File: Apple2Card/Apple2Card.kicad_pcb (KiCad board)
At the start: 2 copper layers, 160 x 78.2 mm, 60 parts, among them J1 ICSP, J2 Conn_01x25, J3 Conn_01x25, J4 Conn_01x16, J5 Conn_01x08, J6 WIZNET 5500, SW1 SW_Push, U1 ATmega328P-P, U3 74HCT00, U4 82C55A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

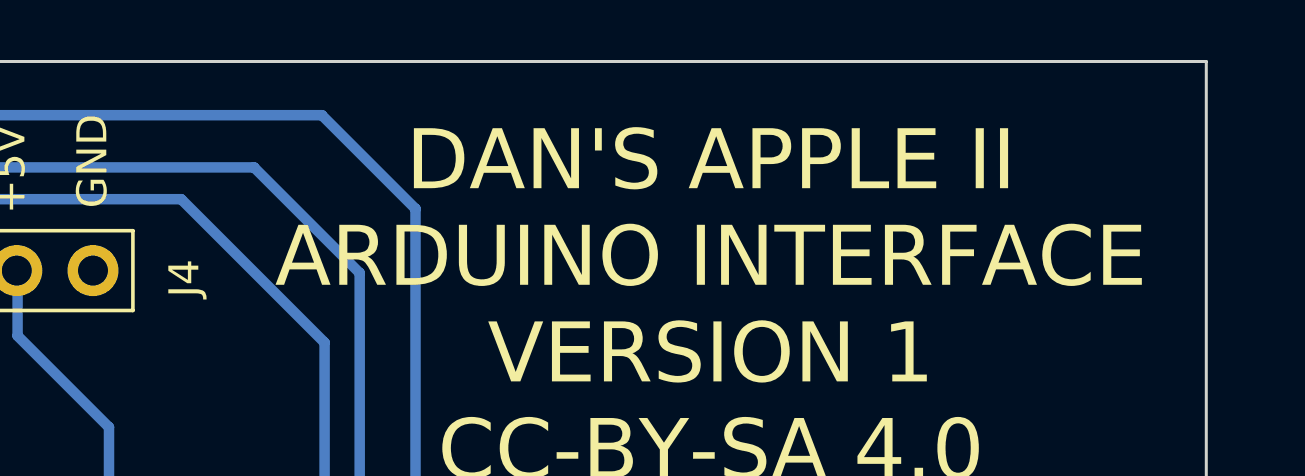
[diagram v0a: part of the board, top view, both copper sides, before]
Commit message: Fixed memory overallocation problem in Arduinosketch
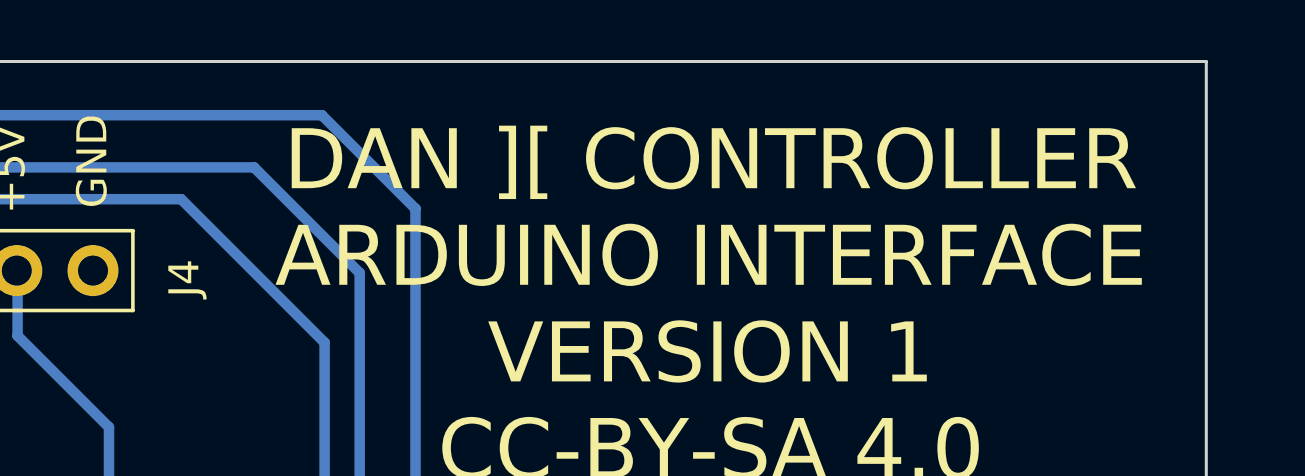
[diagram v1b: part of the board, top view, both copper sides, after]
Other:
- board text added: "DAN ][ CONTROLLER ARDUINO INTERFACE VERSION 1 CC-BY-SA 4.0"
- board text removed: "DAN'S APPLE II ARDUINO INTERFACE VERSION 1 CC-BY-SA 4.0"
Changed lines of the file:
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@@
     (effects (font (size 1 1) (thickness 0.15)))
   )
-  (gr_text "DAN'S APPLE II\nARDUINO INTERFACE\nVERSION 1\nCC-BY-SA 4.0" (at 176.53 33.528) (layer "F.SilkS")
+  (gr_text "DAN ][ CONTROLLER\nARDUINO INTERFACE\nVERSION 1\nCC-BY-SA 4.0" (at 176.53 33.528) (layer "F.SilkS")
     (effects (font (size 2 2) (thickness 0.25)))
   )

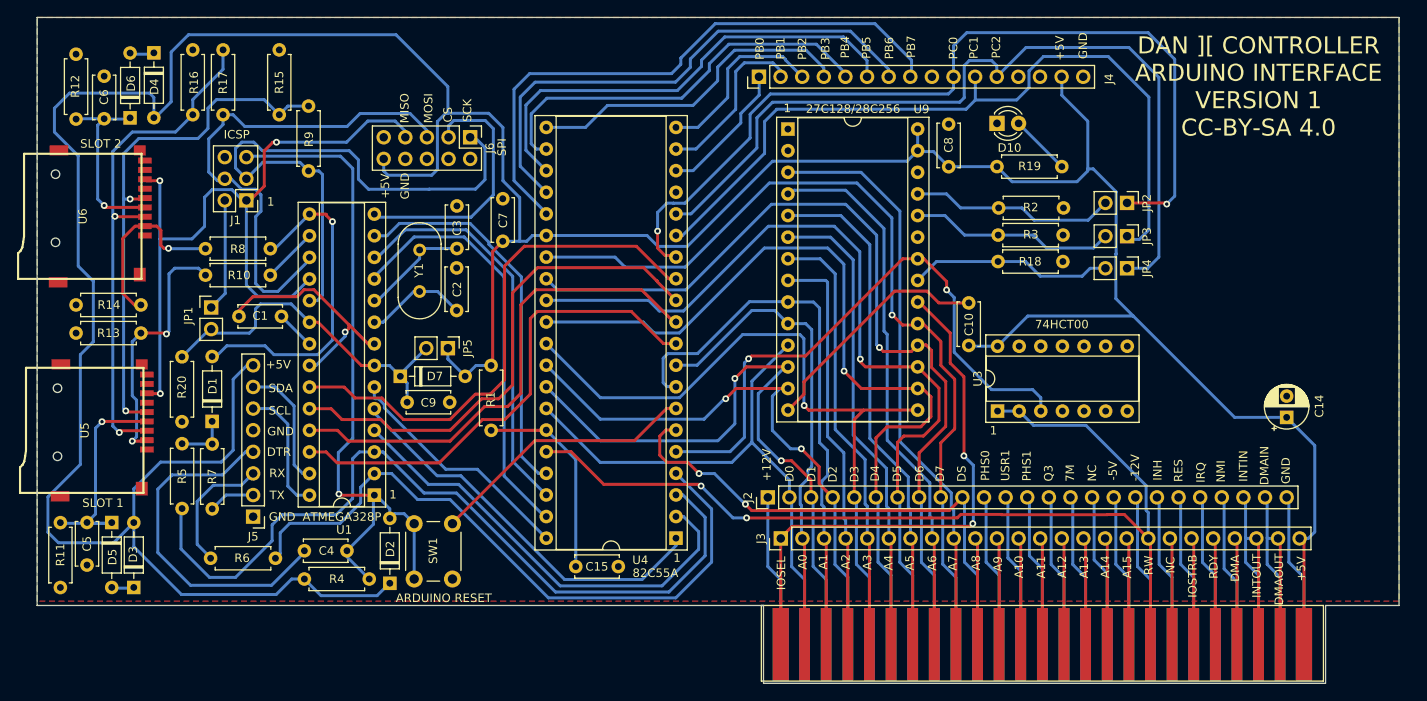
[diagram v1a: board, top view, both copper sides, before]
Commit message: Fixed reset circuitry
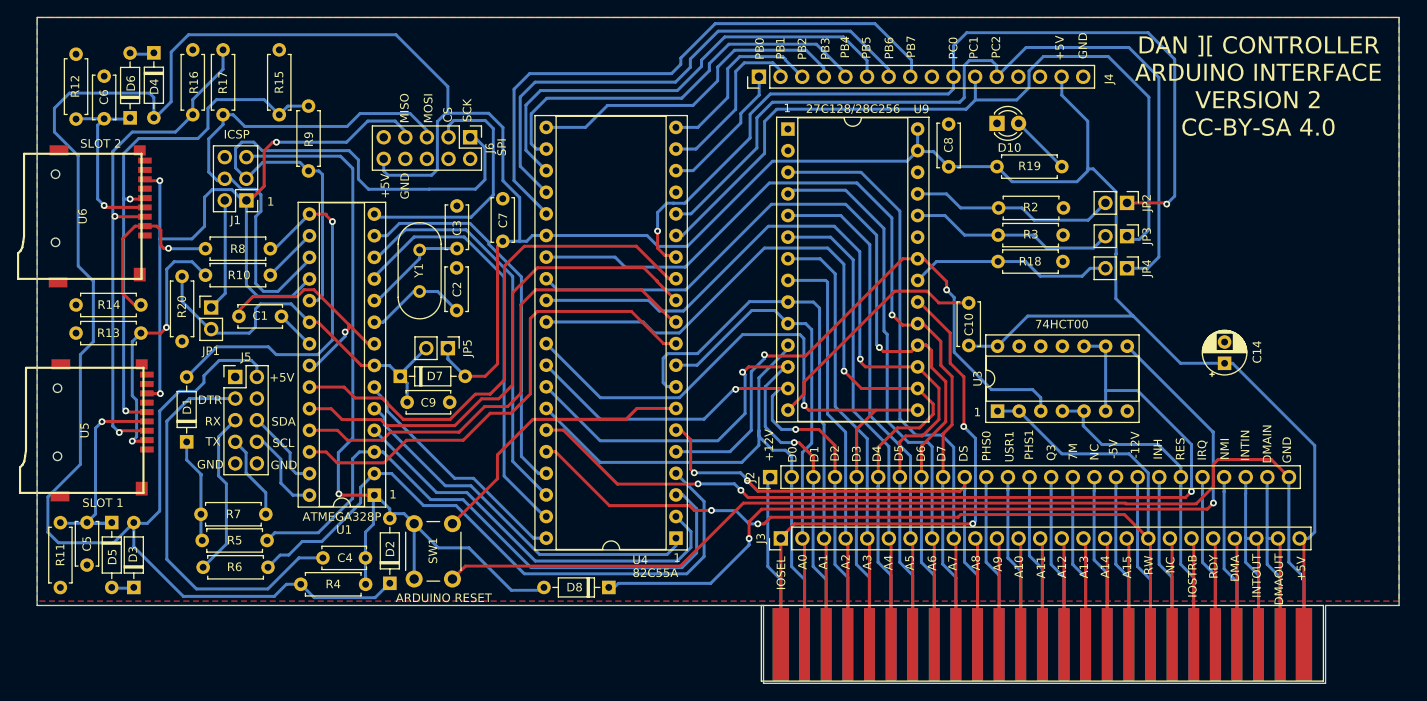
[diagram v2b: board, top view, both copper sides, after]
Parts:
- removed C15: 100 nF, Capacitor_THT:C_Disc_D5.0mm_W2.5mm_P5.00mm
- removed R1: 1k, Resistor_THT:R_Axial_DIN0207_L6.3mm_D2.5mm_P7.62mm_Horizontal
- added D8: 1N4148, Diode_THT:D_DO-35_SOD27_P7.62mm_Horizontal, F.Cu at (100.2, 92.4)
- C4: value 100 nF -> 10 nF
- J5: value Conn_01x08 -> SERCON; footprint Connector_PinHeader_2.54mm:PinHeader_1x08_P2.54mm_Vertical -> Connector_PinHeader_2.54mm:PinHeader_2x05_P2.54mm_Vertical
- R4: value 10k -> 100k
- moved J5 16.5 mm to (56.3, 67.6), turned to 0 degrees
- moved R5 11.6 mm to (52.4, 86.8), turned to 0 degrees
- moved C14 9.67 mm to (172.5, 66.0)
- moved R20 9.45 mm to (50.0, 63.5)
- moved R7 6.33 mm to (59.9, 83.8), turned to 180 degrees
- moved D1 3.84 mm to (50.6, 75.3)
- moved J2 2.39 mm to (119.1, 79.4)
- moved C4 2.34 mm to (66.6, 88.9)
- moved R6 1.37 mm to (52.5, 90.0)
- moved R4 0.75 mm to (64.0, 92.0)
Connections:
- BUS1 pad 31: Net-(BUS1-Pad31) -> RES
- J2 pad 20: Net-(BUS1-Pad31) -> RES
- J5 pad 1: GND -> unconnected-(J5-Pad1)
- J5 pad 2: Net-(J5-Pad2) -> +5V
- J5 pad 3: Net-(J5-Pad3) -> Net-(C4-Pad1)
- J5 pad 4: Net-(C4-Pad1) -> unconnected-(J5-Pad4)
- J5 pad 5: GND -> Net-(R6-Pad1)
- J5 pad 6: PC5 -> PC4
- J5 pad 7: PC4 -> Net-(R7-Pad1)
- J5 pad 8: +5V -> PC5
- R6 pad 1: Net-(J5-Pad3) -> Net-(R6-Pad1)
- R7 pad 1: Net-(J5-Pad2) -> Net-(R7-Pad1)
- U3 pad 10: GND -> Net-(U4-Pad35)
- U3 pad 4: GND -> RES
- U3 pad 5: GND -> RES
- U3 pad 6: unconnected-(U3-Pad6) -> Net-(U4-Pad35)
- U3 pad 8: unconnected-(U3-Pad8) -> Net-(U3-Pad8)
- U3 pad 9: GND -> Net-(U4-Pad35)
- U4 pad 35: Net-(C15-Pad1) -> Net-(U4-Pad35)
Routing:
- net GND: track 105.9 -> 216.3 mm
- net Net-(U4-Pad35): track 0.00 -> 107.8 mm, vias 0 -> 3
- net Net-(U3-Pad8): track 0.00 -> 99.4 mm, vias 0 -> 2
- net RES: track 0.00 -> 39.3 mm
- net Net-(C15-Pad1): track 24.0 -> 0.00 mm
- net PD1: track 95.3 -> 72.2 mm
- net Net-(R6-Pad1): track 0.00 -> 19.6 mm
- net Net-(BUS1-Pad31): track 18.0 -> 0.00 mm
- net RESET: track 81.9 -> 99.2 mm
- net Net-(J5-Pad3): track 15.3 -> 0.00 mm
- net Net-(R7-Pad1): track 0.00 -> 10.00 mm
- net Net-(D1-Pad1): track 6.22 -> 12.4 mm
- net Net-(C4-Pad1): track 41.1 -> 46.7 mm
- net Net-(J5-Pad2): track 5.48 -> 0.00 mm
- net PC4: track 14.9 -> 9.80 mm
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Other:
- board text added: "DAN ][ CONTROLLER ARDUINO INTERFACE VERSION 2 CC-BY-SA 4.0"
- board text removed: "DAN ][ CONTROLLER ARDUINO INTERFACE VERSION 1 CC-BY-SA 4.0"

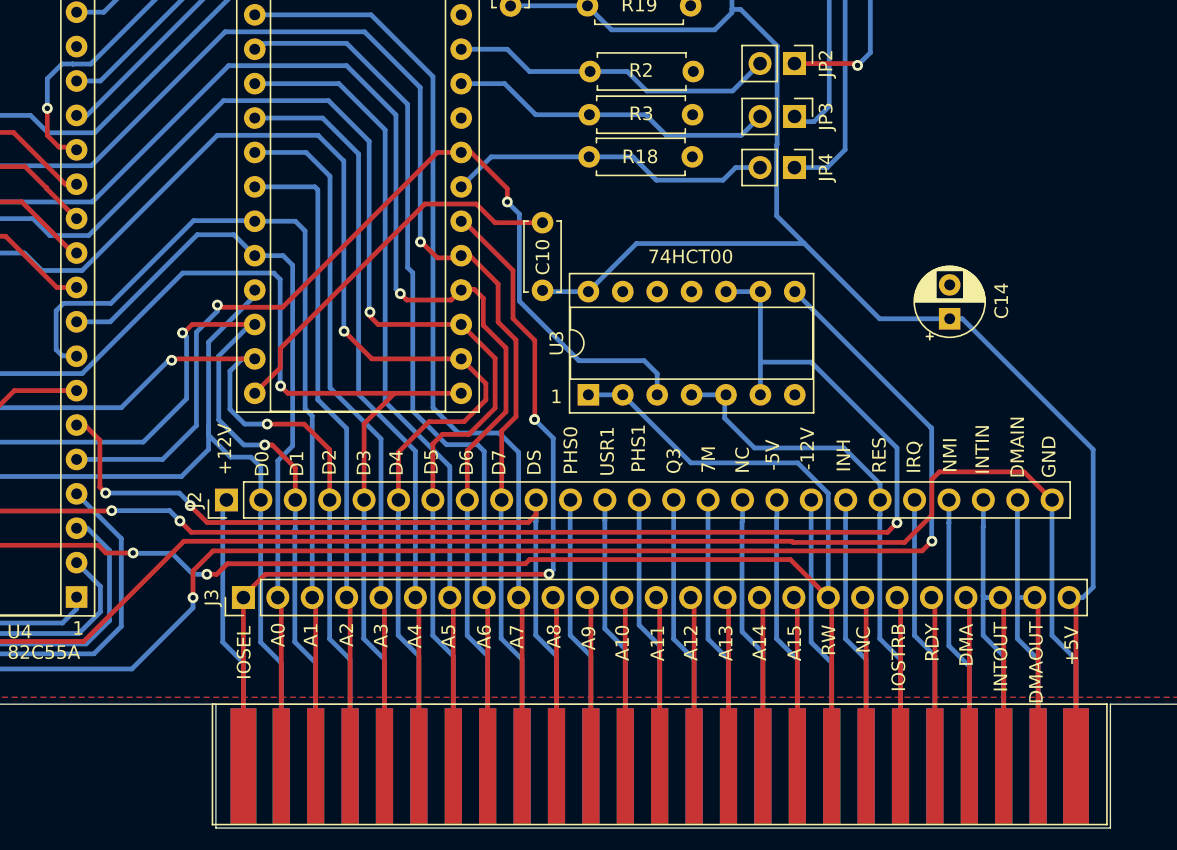
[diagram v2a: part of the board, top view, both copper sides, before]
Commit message: Added code to firmware for bank select
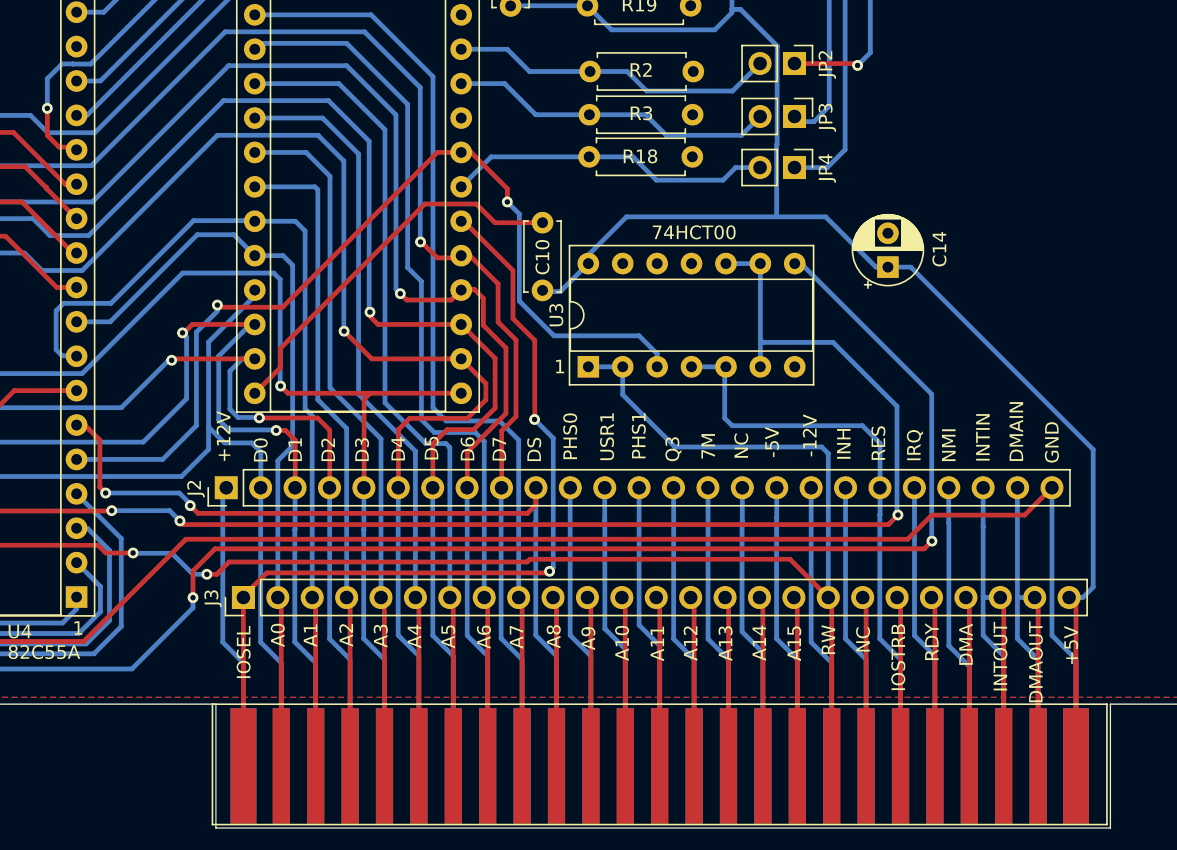
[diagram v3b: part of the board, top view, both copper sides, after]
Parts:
- moved C14 5.95 mm to (168.0, 62.2)
- moved U3 2.07 mm to (145.9, 69.6)
- moved J2 0.90 mm to (119.1, 78.5)
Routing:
- net RES: track 39.3 -> 43.1 mm
- net RW: track 116.8 -> 120.6 mm
- net Net-(U3-Pad8): track 99.4 -> 101.7 mm
- net GND: track 216.3 -> 214.2 mm
- net Net-(U4-Pad35): track 107.8 -> 109.6 mm
- net Net-(U3-Pad3): track 69.4 -> 68.1 mm
- net D1: track 76.0 -> 77.2 mm
- net D4: track 98.1 -> 99.1 mm
- net Net-(BUS1-Pad39): track 20.3 -> 21.2 mm
- net Net-(BUS1-Pad37): track 20.3 -> 21.2 mm
- net Net-(BUS1-Pad30): track 20.3 -> 21.2 mm
- net Net-(BUS1-Pad36): track 20.3 -> 21.2 mm
- net Net-(BUS1-Pad29): track 20.3 -> 21.2 mm
- net Net-(BUS1-Pad24): track 34.1 -> 35.0 mm
- net Net-(BUS1-Pad40): track 20.3 -> 21.2 mm
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
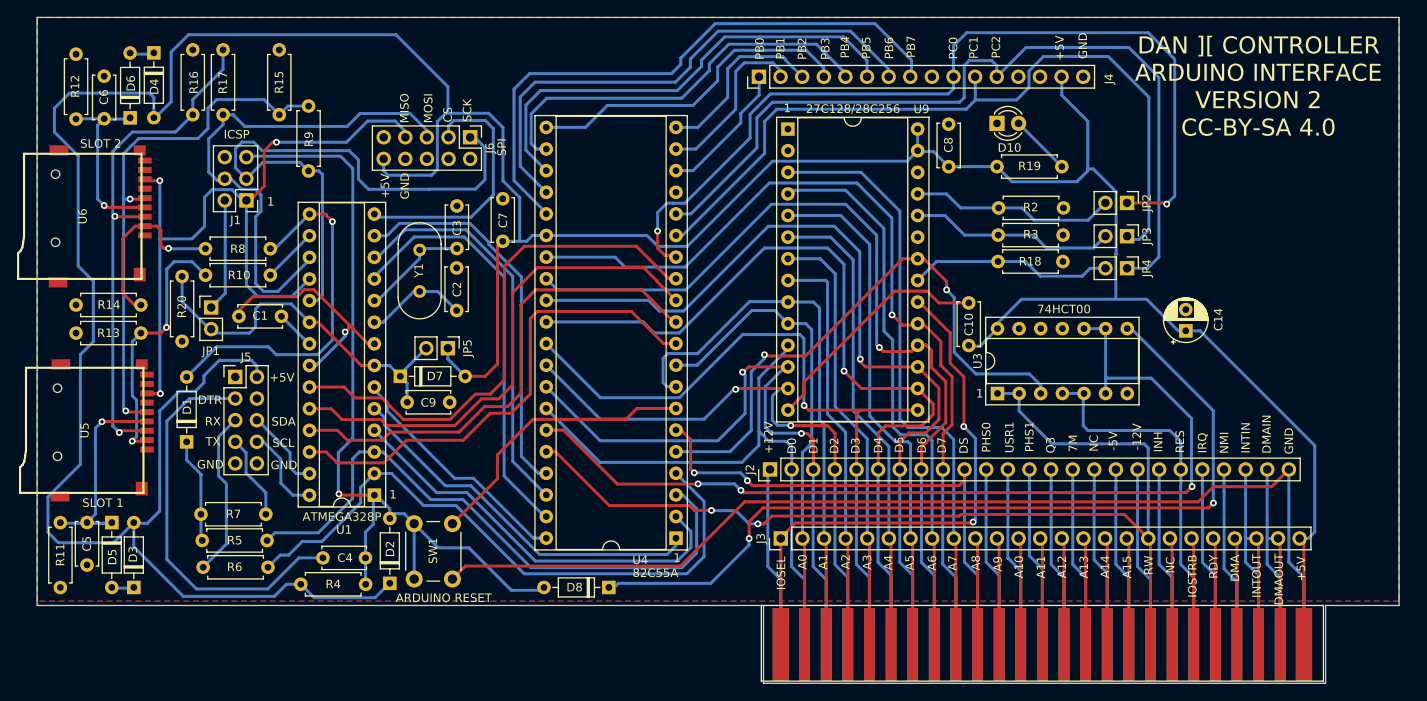
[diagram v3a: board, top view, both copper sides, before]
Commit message: Both slots working with real hardwarE
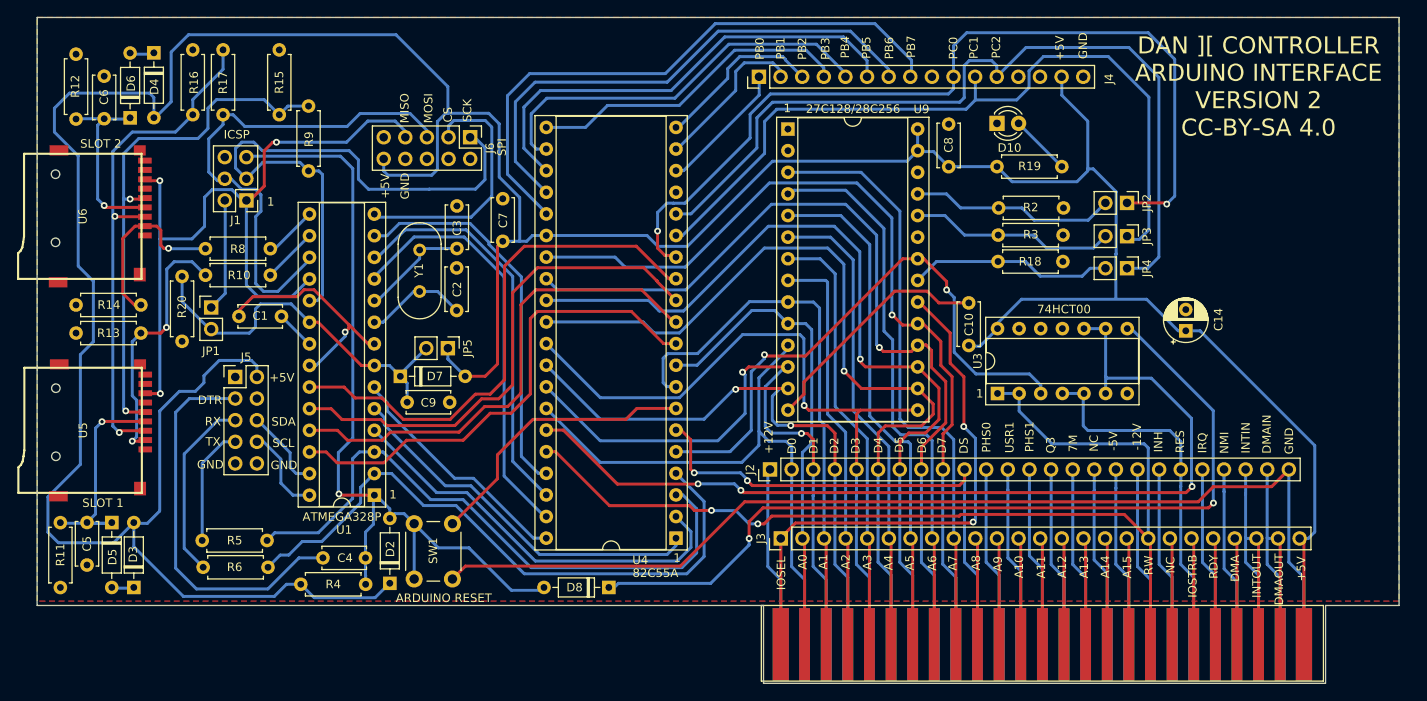
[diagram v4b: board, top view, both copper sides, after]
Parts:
- removed D1: 1N4148, Diode_THT:D_DO-35_SOD27_P7.62mm_Horizontal
- removed R7: 2k2, Resistor_THT:R_Axial_DIN0207_L6.3mm_D2.5mm_P7.62mm_Horizontal
- C4: value 10 nF -> 100 nF
- R4: value 100k -> 10k
- moved U5 0.19 mm to (46.5, 73.9)
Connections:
- J5 pad 7: Net-(R7-Pad1) -> Net-(J5-Pad7)
- R5 pad 1: Net-(D1-Pad1) -> Net-(J5-Pad7)
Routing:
- net CS2: track 43.0 -> 6.28 mm, vias 1 -> 0
- net Net-(J5-Pad7): track 0.00 -> 14.0 mm
- net Net-(D1-Pad1): track 12.4 -> 0.00 mm
- net Net-(R7-Pad1): track 10.00 -> 0.00 mm
- net Net-(J5-Pad5): track 19.6 -> 21.9 mm
- net Net-(J4-Pad3): track 21.3 -> 20.0 mm
- net Net-(J4-Pad2): track 20.2 -> 18.9 mm
- net Net-(J4-Pad4): track 39.2 -> 38.3 mm
- net Net-(C4-Pad1): track 46.7 -> 45.8 mm
- net Net-(J4-Pad1): track 16.3 -> 15.6 mm
